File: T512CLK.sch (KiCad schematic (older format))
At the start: 60 parts, among them J1 Bus_ISA_8bit, U1 41256, U10 41256, U11 41256, U12 41256, U13 41256, U14 41256, U15 41256, U16 41256, U17 74LS139, U18 74LS08, U19 74LS32, U2 41256, U20 74LS258, U21 74LS258, U22 RTC, U23 74LS138, U24 74LS373, U25 8237A, U26 74LS245, U27 74LS74, U28 74LS04, U29 74LS245, U3 41256, U30 74LS670, U31 74LS00, U32 74LS74, U4 41256, U5 41256, U6 41256, U7 41256, U8 41256, U9 41256

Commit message: Change RP3 symbol from a single to split for better readability.
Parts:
- removed RP3: 4K7 Bussed, Resistor_THT:R_Array_SIP8, symbol Device:R_Network07
- added RP3: 4K7 Bussed, Resistor_THT:R_Array_SIP8, symbol Device:R_Network07_Split
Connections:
- net DMA_READY_IN: now also RP3.6 (R5.2)
- net VCC: now also RP3.1 (R1.1)
- net ~EOP: now also RP3.7 (R6.2)
- net A0_DRV renamed A0_BUF
- net A1_DRV renamed A1_BUF
- net A2_DRV renamed A2_BUF
- net A3_DRV renamed A3_BUF
- net ~IOR~_DRV renamed ~IOR~_BUF
- net ~IOR~_BUF: now also RP3.2 (R1.2)
- net ~IOW~_DRV renamed ~IOW~_BUF
- net ~IOW~_BUF: now also RP3.3 (R2.2)
- net ~MEMR~_DRV renamed ~MEMR~_BUF
- net ~MEMR~_BUF: now also RP3.4 (R3.2)
- net ~MEMW~_DRV renamed ~MEMW~_BUF
- net ~MEMW~_BUF: now also RP3.5 (R4.2)
- no-connect marks 47 -> 46
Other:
- moved on the sheet: U31A, U31C, U31D, U32A, U32B

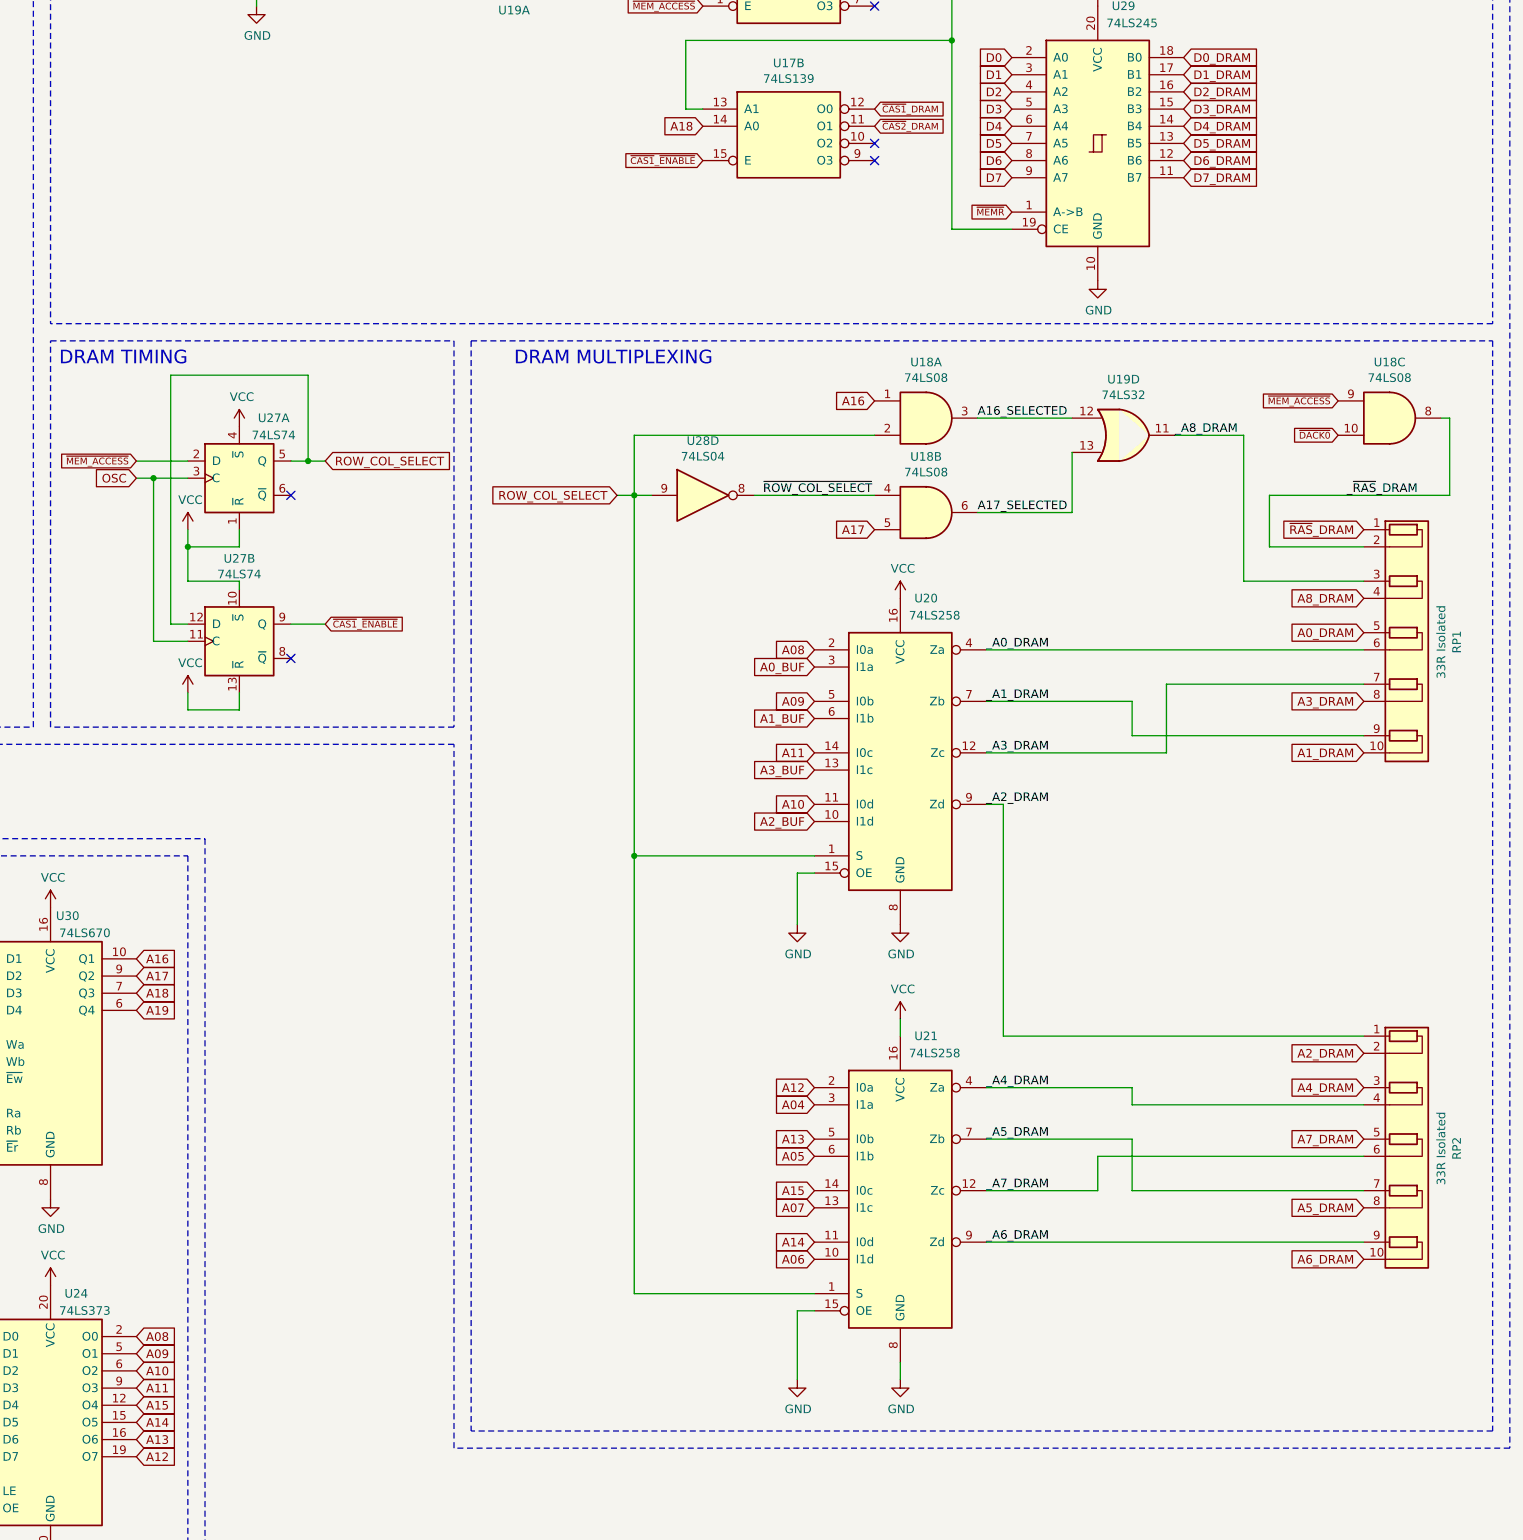
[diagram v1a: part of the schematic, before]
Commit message: Change RP1 and RP2 symbols from single to split for better readability.
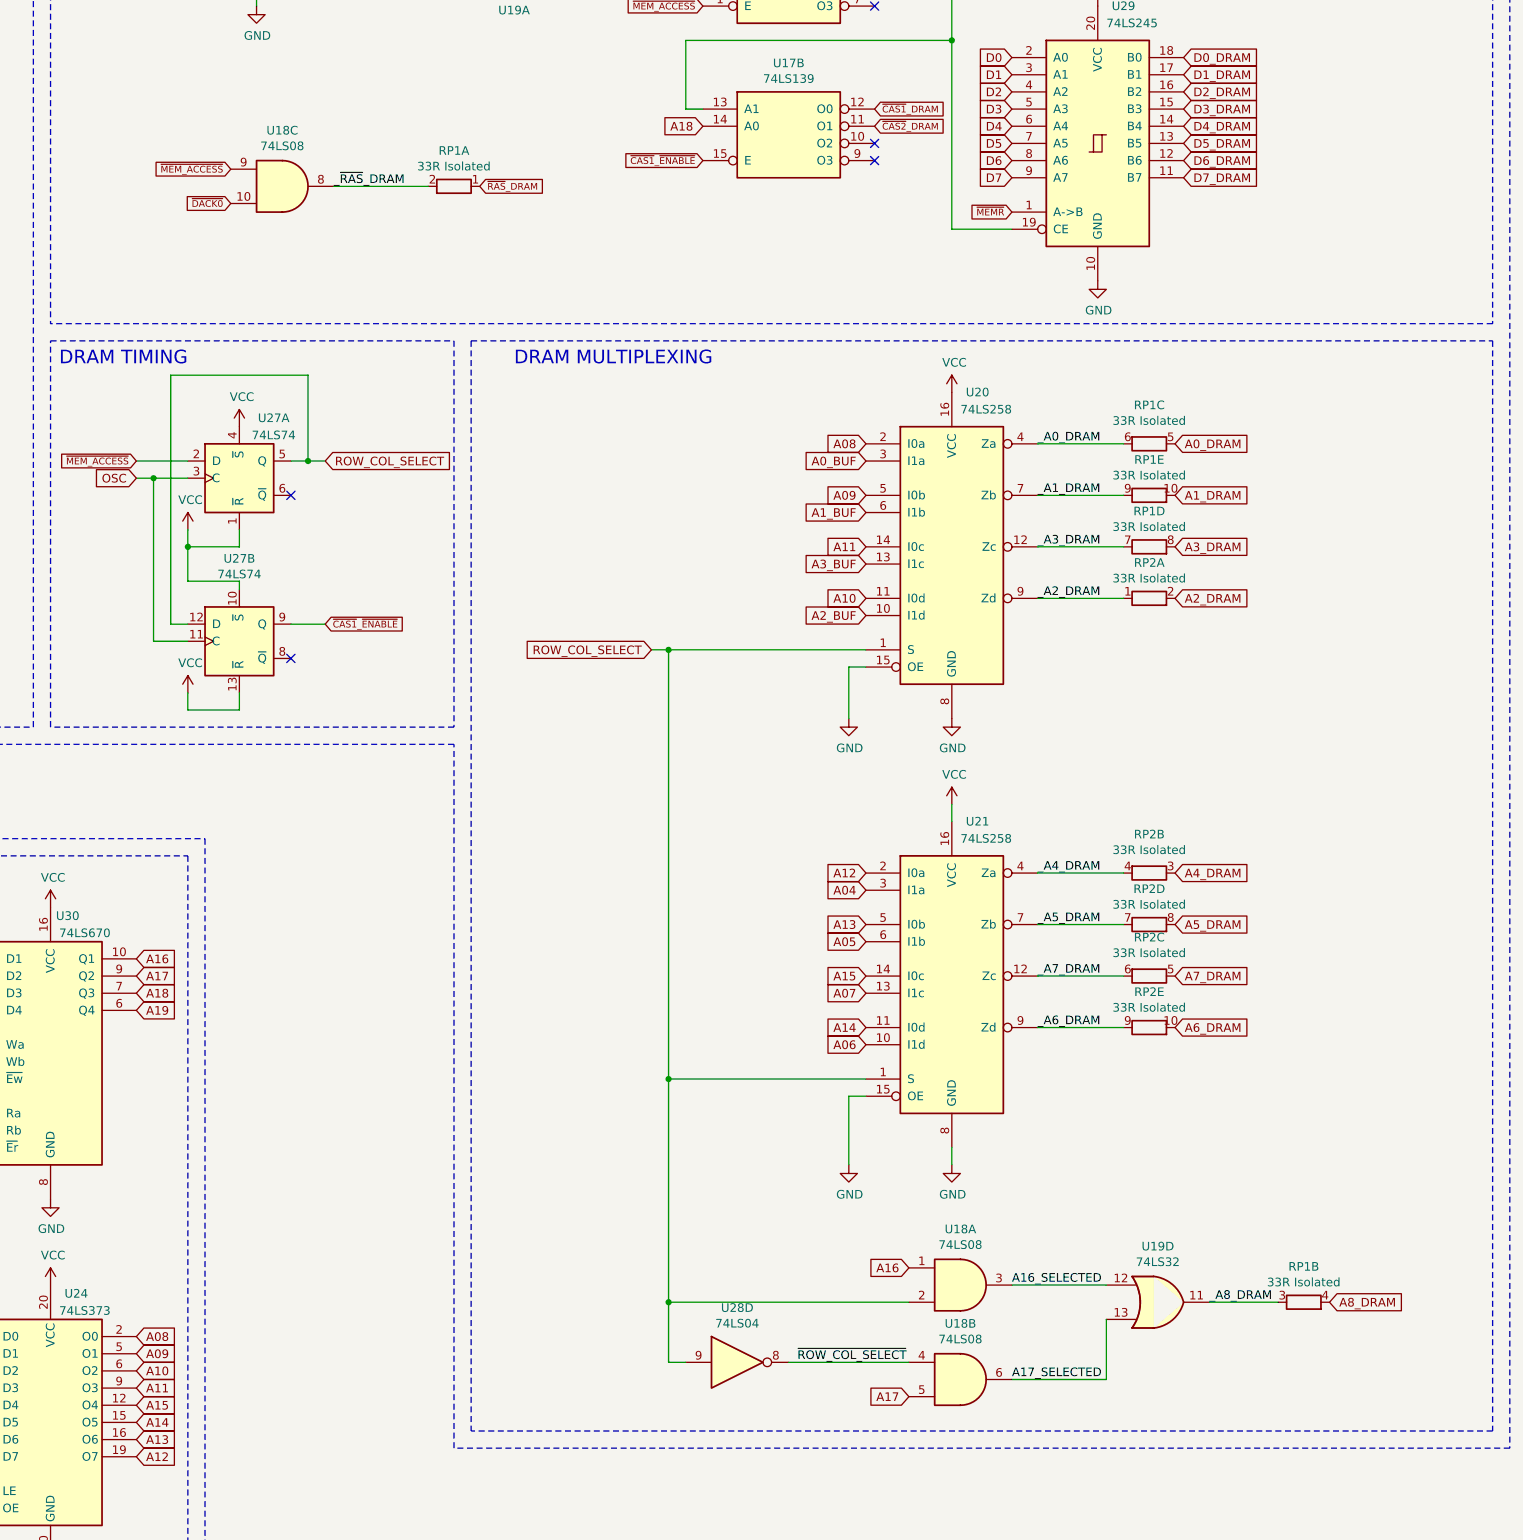
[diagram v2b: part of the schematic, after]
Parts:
- removed RP1, RP2: 33R Isolated, Resistor_THT:R_Array_SIP10, symbol Device:R_Pack05_SIP
- added RP1, RP2: 33R Isolated, Resistor_THT:R_Array_SIP10, symbol Device:R_Pack05_SIP_Split
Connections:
- net A0_DRAM: now also RP1.5 (R3.1)
- net A1_DRAM: now also RP1.10 (R5.2)
- net A2_DRAM: now also RP2.2 (R1.2)
- net A3_DRAM: now also RP1.8 (R4.2)
- net A4_DRAM: now also RP2.3 (R2.1)
- net A5_DRAM: now also RP2.8 (R4.2)
- net A6_DRAM: now also RP2.10 (R5.2)
- net A7_DRAM: now also RP2.5 (R3.1)
- net A8_DRAM: now also RP1.4 (R2.2)
- net _A0_DRAM: now also RP1.6 (R3.2)
- net _A1_DRAM: now also RP1.9 (R5.1)
- net _A2_DRAM: now also RP2.1 (R1.1)
- net _A3_DRAM: now also RP1.7 (R4.1)
- net _A4_DRAM: now also RP2.4 (R2.2)
- net _A5_DRAM: now also RP2.7 (R4.1)
- net _A6_DRAM: now also RP2.9 (R5.1)
- net _A7_DRAM: now also RP2.6 (R3.2)
- net _A8_DRAM: now also RP1.3 (R2.1)
- net _~RAS~_DRAM: now also RP1.2 (R1.2)
- net ~RAS~_DRAM: now also RP1.1 (R1.1)
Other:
- moved on the sheet: U18A, U18B, U18C, U19D, U20, U21, U28D
